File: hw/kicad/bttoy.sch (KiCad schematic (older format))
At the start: 4 parts

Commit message: - start flushing out subsystems
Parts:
- added C? (x2): 4.7uF, symbol C
- added C? (x2): 1uF, symbol C
- added D?: LED, symbol LED
- added J?: ARM_10PIN, symbol ARM_10PIN
- added J?: HC-07_BLUETOOTH, symbol HC-07_BLUETOOTH
- added P?: MOTOR+, symbol TST
- added P?: MOTOR-, symbol TST
- added Q? (x4): MOSFET_N, symbol MOSFET_N
- added R?: 1K, symbol R
- added R?: 2K, symbol R
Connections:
- net +3.3v: now reaches U?.3 (VDD)
- net +3.3v: now also U?.5 (OUT), C?.1, J?.1 (VCC)
- net swd_clk: now reaches U?.30 (PTA0/SWD_CLK)
- net swd_clk: now also J?.4 (SWCLK/TCLK)
- net nreset: now reaches U?.31 (PTA1/RESET_b)
- net nreset: now also J?.10 (nRESET)
- net swd_io: now reaches U?.32 (PTA2/SWD_IO)
- net swd_io: now also J?.2 (SWDIO/TMS)
- net GND: now reaches U?.6 (VSS)
- net GND: now also J?.5 (GND), J?.6 (SHIELD), U?.2 (GND), U?.2 (vss), C?.2, C?.2, C?.2, C?.2, J?.3 (GND), J?.5 (GND), J?.9 (GND), Q?.S, Q?.S, R?.2
- net at U?.1 (stat): now also R?.2
- net batt+: now reaches U?.3 (vbat)
- net batt+: now also U?.1 (IN), U?.3 (EN), C?.1, C?.1
- net usb_vbus: now reaches U?.4 (vdd)
- net usb_vbus: now also J?.1 (VBUS), C?.1, D?.1 (A)
- net at U?.5 (prog): now also R?.1
- new net: J?.22 (GND), P?.1, Q?.D, Q?.S
- new net: P?.1, Q?.D, Q?.S
- new net: D?.2 (K), R?.1
- new net +9V: Q?.D, Q?.D
- new net A1: Q?.G
- new net A2: Q?.G
- new net B1: Q?.G
- new net B2: Q?.G
- no-connect marks 0 -> 7
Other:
- note added: "CHARGER"
- note added: "DEBUG HEADER"
- note added: "LOGIC POWER SUPPLY"
- note added: "MOTOR CONTROL"
- note added: "USB CONNECTOR"
- moved on the sheet: J?, U?

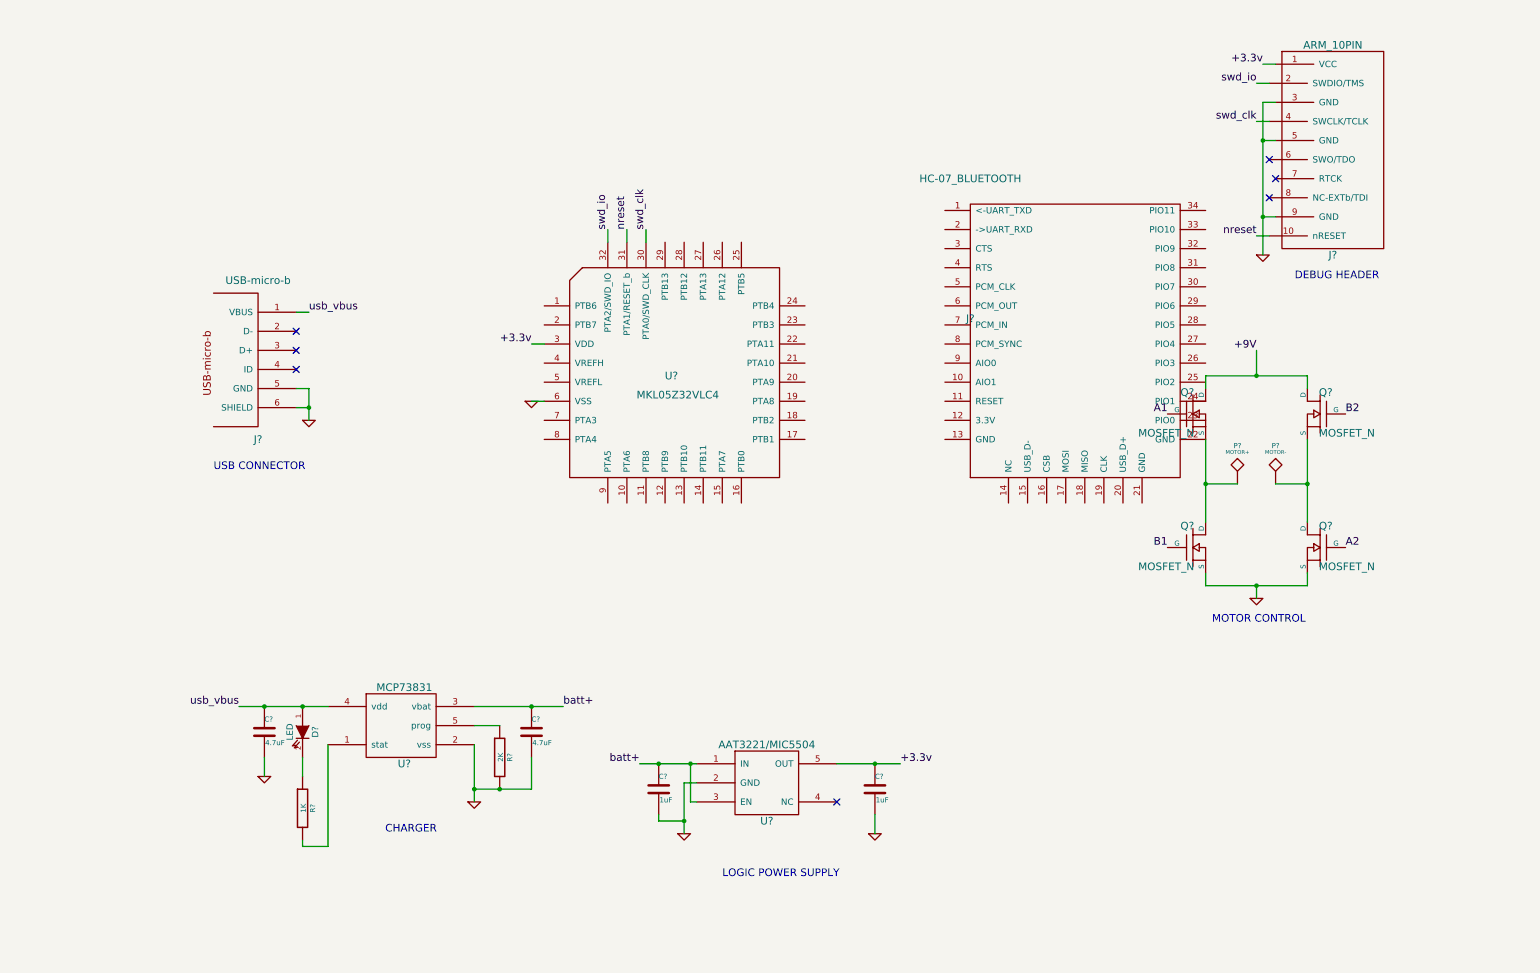
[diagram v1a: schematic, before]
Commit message: - flesh out schematic, add MPS using MIC2288 boost controller
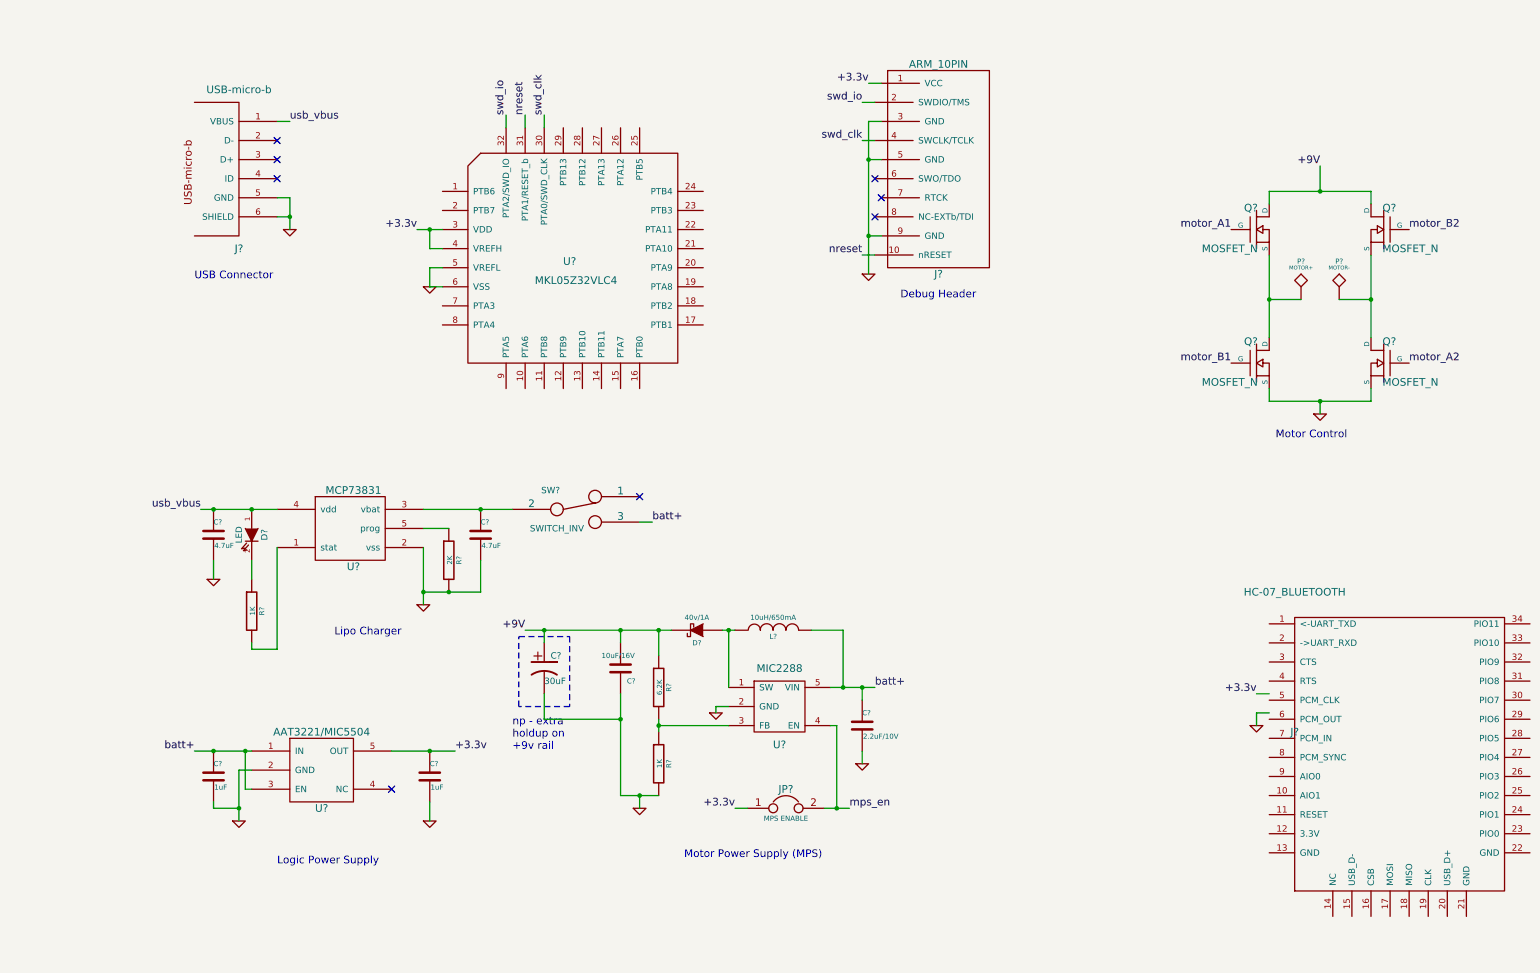
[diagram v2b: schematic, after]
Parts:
- added C?: 2.2uF/10V, symbol C
- added C?: 10uF/16V, symbol C
- added C?: 30uF, symbol CP1
- added D?: 40v/1A, symbol DIODESCH
- added JP?: MPS ENABLE, symbol JUMPER
- added L?: 10uH/650mA, symbol INDUCTOR
- added R?: 6.2K, symbol R
- added R?: 1K, symbol R
- added SW?: SWITCH_INV, symbol SWITCH_INV
- added U?: MIC2288, symbol MIC2288
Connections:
- net +3.3v: now also U?.4 (VREFH), JP?.1
- net +9V: now also C?.1, C?.1, D?.2 (K), R?.1
- net GND: now also U?.5 (VREFL), C?.2, C?.2, C?.2, R?.2, U?.2 (GND)
- net batt+: now also C?.1, L?.2, SW?.3, U?.5 (VIN); no longer C?.1, U?.3 (vbat)
- net at P?.1, Q?.D, Q?.S: no longer J?.22 (GND)
- net A1 renamed motor_A1
- net A2 renamed motor_A2
- net B1 renamed motor_B1
- net B2 renamed motor_B2
- new net: C?.1, SW?.2, U?.3 (vbat)
- new net: D?.1 (A), L?.1, U?.1 (SW)
- new net: R?.1, R?.2, U?.3 (FB)
- new net mps_en: JP?.2, U?.4 (EN)
- no-connect marks 7 -> 8
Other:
- note added: "Debug Header"
- note added: "Lipo Charger"
- note added: "Logic Power Supply"
- note added: "Motor Control"
- note added: "Motor Power Supply (MPS)"
- note added: "USB Connector"
- note added: "np - extra\nholdup on\n+9v rail"
- note removed: "CHARGER"
- note removed: "DEBUG HEADER"
- note removed: "LOGIC POWER SUPPLY"
- note removed: "MOTOR CONTROL"
- note removed: "USB CONNECTOR"
- moved on the sheet: C?, D?, J?, P?, Q?, R?, U?

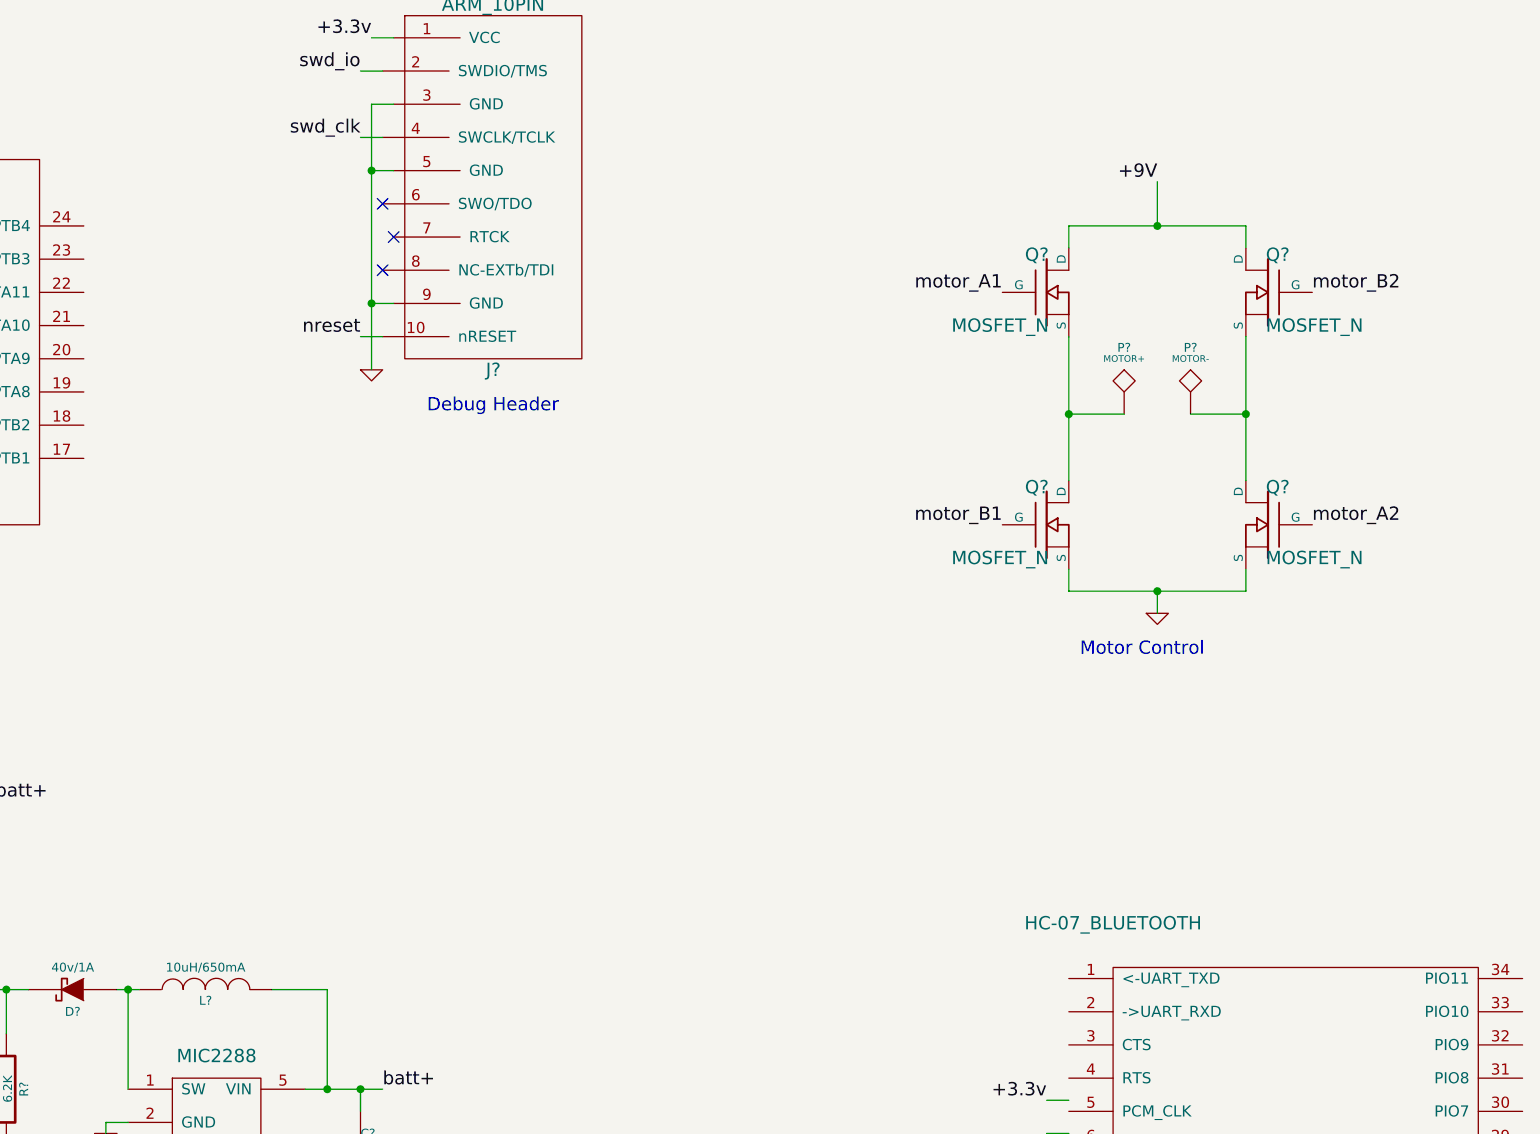
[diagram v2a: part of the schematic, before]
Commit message: - add reference part # for inductor
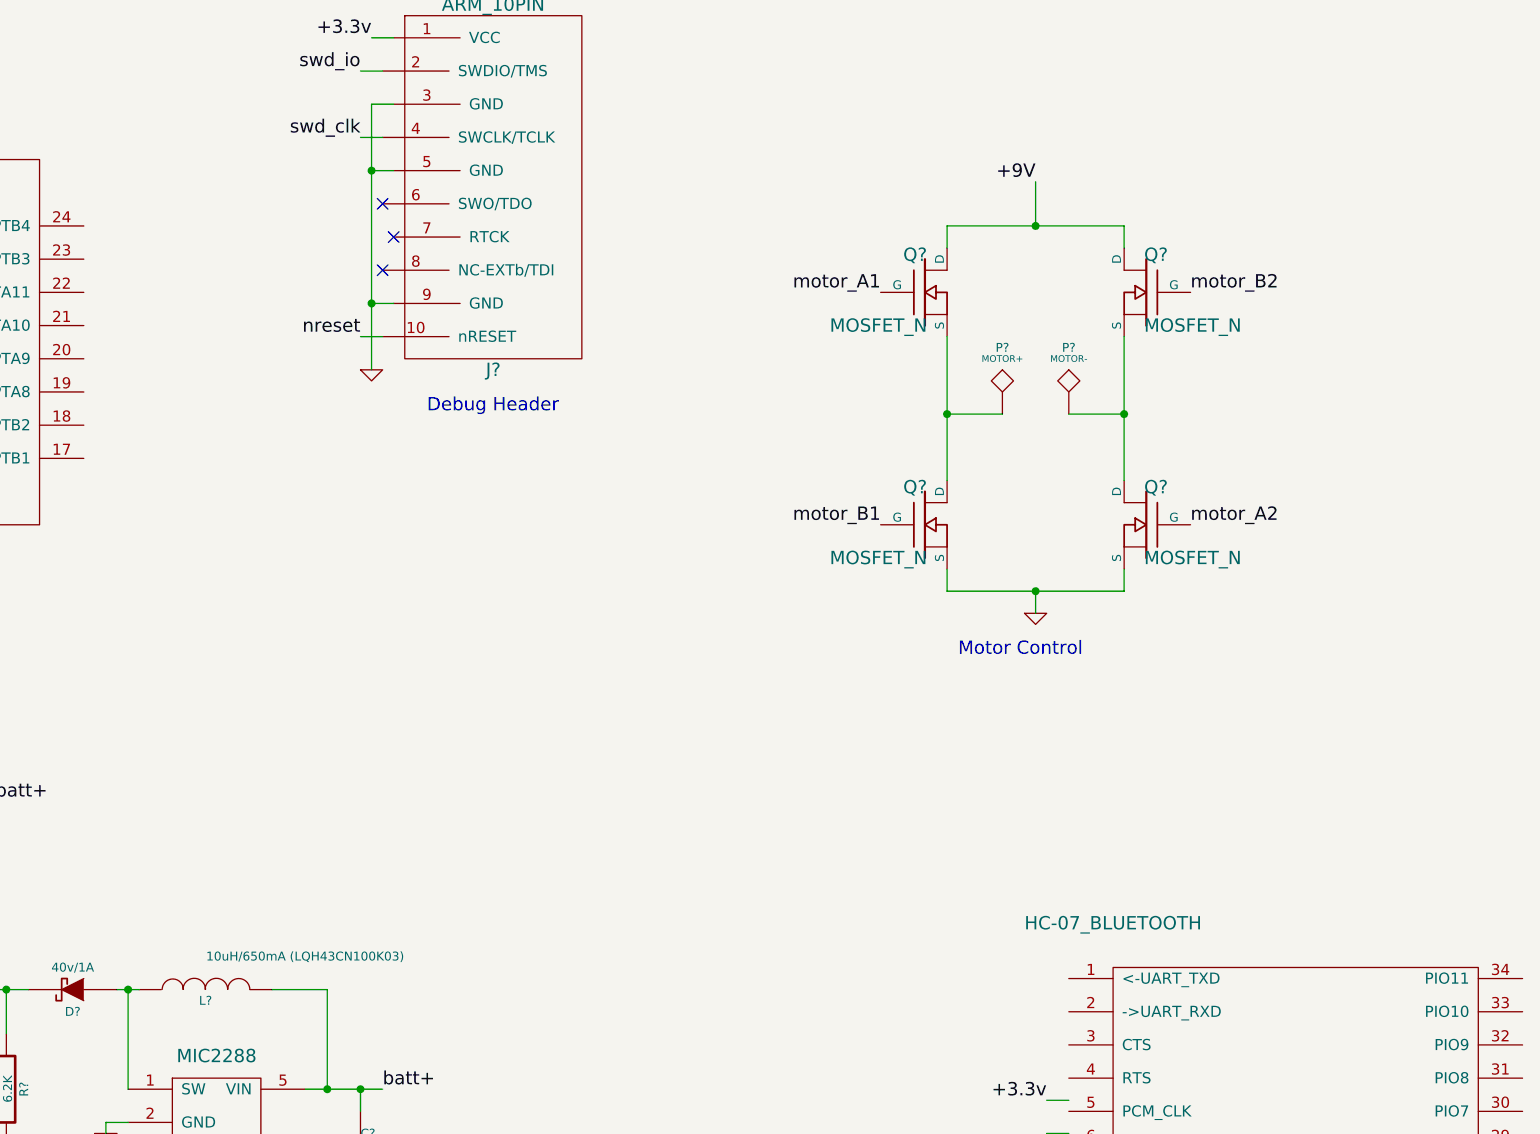
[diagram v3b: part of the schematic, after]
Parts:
- L?: value 10uH/650mA -> 10uH/650mA (LQH43CN100K03)
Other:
- moved on the sheet: P?, Q?
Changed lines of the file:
@@
 EELAYER 25 0
 EELAYER END
-$Descr A4 11693 8268
+$Descr USLetter 11000 8500
 encoding utf-8
 Sheet 1 1
@@
 L MOSFET_N Q?
 U 1 1 54A96EB2
-P 9250 2100
-F 0 "Q?" H 9260 2270 60  0000 R CNN
-F 1 "MOSFET_N" H 9260 1950 60  0000 R CNN
-F 2 "" H 9250 2100 60  0000 C CNN
-F 3 "" H 9250 2100 60  0000 C CNN
-	1    9250 2100
+P 8700 2100
+F 0 "Q?" H 8710 2270 60  0000 R CNN
+F 1 "MOSFET_N" H 8710 1950 60  0000 R CNN
+F 2 "" H 8700 2100 60  0000 C CNN
+F 3 "" H 8700 2100 60  0000 C CNN
+	1    8700 2100
 	1    0    0    -1
 $EndComp
@@
 L MOSFET_N Q?
 U 1 1 54A96F0B
-P 10250 2100
-F 0 "Q?" H 10260 2270 60  0000 R CNN
-F 1 "MOSFET_N" H 10260 1950 60  0000 R CNN
-F 2 "" H 10250 2100 60  0000 C CNN
-F 3 "" H 10250 2100 60  0000 C CNN
-	1    10250 2100
+P 9700 2100
+F 0 "Q?" H 9710 2270 60  0000 R CNN
+F 1 "MOSFET_N" H 9710 1950 60  0000 R CNN
+F 2 "" H 9700 2100 60  0000 C CNN
+F 3 "" H 9700 2100 60  0000 C CNN
+	1    9700 2100
 	-1   0    0    -1
 $EndComp
@@
 L MOSFET_N Q?
 U 1 1 54A97086
-P 10250 3150
-F 0 "Q?" H 10260 3320 60  0000 R CNN
-F 1 "MOSFET_N" H 10260 3000 60  0000 R CNN
-F 2 "" H 10250 3150 60  0000 C CNN
-F 3 "" H 10250 3150 60  0000 C CNN
-	1    10250 3150
+P 9700 3150
+F 0 "Q?" H 9710 3320 60  0000 R CNN
+F 1 "MOSFET_N" H 9710 3000 60  0000 R CNN
+F 2 "" H 9700 3150 60  0000 C CNN
+F 3 "" H 9700 3150 60  0000 C CNN
+	1    9700 3150
 	-1   0    0    -1
 $EndComp
@@
 L MOSFET_N Q?
 U 1 1 54A970C7
-P 9250 3150
-F 0 "Q?" H 9260 3320 60  0000 R CNN
-F 1 "MOSFET_N" H 9260 3000 60  0000 R CNN
-F 2 "" H 9250 3150 60  0000 C CNN
-F 3 "" H 9250 3150 60  0000 C CNN
-	1    9250 3150
+P 8700 3150
+F 0 "Q?" H 8710 3320 60  0000 R CNN
+F 1 "MOSFET_N" H 8710 3000 60  0000 R CNN
+F 2 "" H 8700 3150 60  0000 C CNN
+F 3 "" H 8700 3150 60  0000 C CNN
+	1    8700 3150
 	1    0    0    -1
 $EndComp
@@
 L TST P?
 U 1 1 54A9712B
-P 9600 2650
-F 0 "P?" H 9600 2950 40  0000 C CNN
-F 1 "MOTOR+" H 9600 2900 30  0000 C CNN
-F 2 "" H 9600 2650 60  0000 C CNN
-F 3 "" H 9600 2650 60  0000 C CNN
-	1    9600 2650
+P 9050 2650
+F 0 "P?" H 9050 2950 40  0000 C CNN
+F 1 "MOTOR+" H 9050 2900 30  0000 C CNN
+F 2 "" H 9050 2650 60  0000 C CNN
+F 3 "" H 9050 2650 60  0000 C CNN
+	1    9050 2650
 	1    0    0    -1
 $EndComp
@@
 L TST P?
 U 1 1 54A97184
-P 9900 2650
-F 0 "P?" H 9900 2950 40  0000 C CNN
-F 1 "MOTOR-" H 9900 2900 30  0000 C CNN
-F 2 "" H 9900 2650 60  0000 C CNN
-F 3 "" H 9900 2650 60  0000 C CNN
-	1    9900 2650
-	1    0    0    -1
-$EndComp
-Wire Wire Line
-	9900 2650 10150 2650
-Wire Wire Line
-	10150 2300 10150 2950
-Connection ~ 10150 2650
-Wire Wire Line
-	9600 2650 9350 2650
-Wire Wire Line
-	9350 2300 9350 2950
-Connection ~ 9350 2650
-Text Label 9050 2100 2    60   ~ 0
+P 9350 2650
+F 0 "P?" H 9350 2950 40  0000 C CNN
+F 1 "MOTOR-" H 9350 2900 30  0000 C CNN
+F 2 "" H 9350 2650 60  0000 C CNN
+F 3 "" H 9350 2650 60  0000 C CNN
+	1    9350 2650
+	1    0    0    -1
+$EndComp
+Wire Wire Line
+	9350 2650 9600 2650
+Wire Wire Line
+	9600 2300 9600 2950
+Connection ~ 9600 2650
+Wire Wire Line
+	9050 2650 8800 2650
+Wire Wire Line
+	8800 2300 8800 2950
+Connection ~ 8800 2650
+Text Label 8500 2100 2    60   ~ 0
 motor_A1
-Text Label 10450 3150 0    60   ~ 0
+Text Label 9900 3150 0    60   ~ 0
 motor_A2
-Text Label 10450 2100 0    60   ~ 0
+Text Label 9900 2100 0    60   ~ 0
 motor_B2
-Text Label 9050 3150 2    60   ~ 0
+Text Label 8500 3150 2    60   ~ 0
 motor_B1
 $Comp
 L GND #PWR?
 U 1 1 54A9735F
-P 9750 3550
-F 0 "#PWR?" H 9750 3550 30  0001 C CNN
-F 1 "GND" H 9750 3480 30  0001 C CNN
-F 2 "" H 9750 3550 60  0000 C CNN
-F 3 "" H 9750 3550 60  0000 C CNN
-	1    9750 3550
-	1    0    0    -1
-$EndComp
-Wire Wire Line
-	9350 3350 9350 3450
-Wire Wire Line
-	9350 3450 10150 3450
-Wire Wire Line
-	9750 3450 9750 3550
-Wire Wire Line
-	10150 3450 10150 3350
-Connection ~ 9750 3450
-Wire Wire Line
-	9350 1900 9350 1800
-Wire Wire Line
-	9350 1800 10150 1800
-Wire Wire Line
-	10150 1800 10150 1900
+P 9200 3550
+F 0 "#PWR?" H 9200 3550 30  0001 C CNN
+F 1 "GND" H 9200 3480 30  0001 C CNN
+F 2 "" H 9200 3550 60  0000 C CNN
+F 3 "" H 9200 3550 60  0000 C CNN
+	1    9200 3550
+	1    0    0    -1
+$EndComp
+Wire Wire Line
+	8800 3350 8800 3450
+Wire Wire Line
+	8800 3450 9600 3450
+Wire Wire Line
+	9200 3450 9200 3550
+Wire Wire Line
+	9600 3450 9600 3350
+Connection ~ 9200 3450
+Wire Wire Line
+	8800 1900 8800 1800
+Wire Wire Line
+	8800 1800 9600 1800
+Wire Wire Line
+	9600 1800 9600 1900
 $Comp
 L R R?
@@
 $EndComp
 Wire Wire Line
-	9750 1800 9750 1600
-Connection ~ 9750 1800
-Text Label 9750 1600 2    60   ~ 0
+	9200 1800 9200 1600
+Connection ~ 9200 1800
+Text Label 9200 1600 2    60   ~ 0
 +9V
-Text Notes 9400 3750 0    60   ~ 0
+Text Notes 8850 3750 0    60   ~ 0
 Motor Control
 $Comp
@@
 P 5450 5250
 F 0 "L?" V 5400 5250 40  0000 C CNN
-F 1 "10uH/650mA" V 5550 5250 40  0000 C CNN
+F 1 "10uH/650mA (LQH43CN100K03)" V 5600 4800 40  0000 C CNN
 F 2 "" H 5450 5250 60  0000 C CNN
 F 3 "" H 5450 5250 60  0000 C CNN
